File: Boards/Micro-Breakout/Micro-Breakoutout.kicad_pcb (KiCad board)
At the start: 2 copper layers, 92.7 x 54.6 mm, 38 parts, among them J1 Conn_01x04, J10 Conn_01x17, J11 Conn_01x04, J12 Conn_01x04, J13 Conn_01x02, J14 Conn_01x04, J16 Conn_01x04, J17 Conn_01x04, J18 Conn_01x04, J2 Conn_01x04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

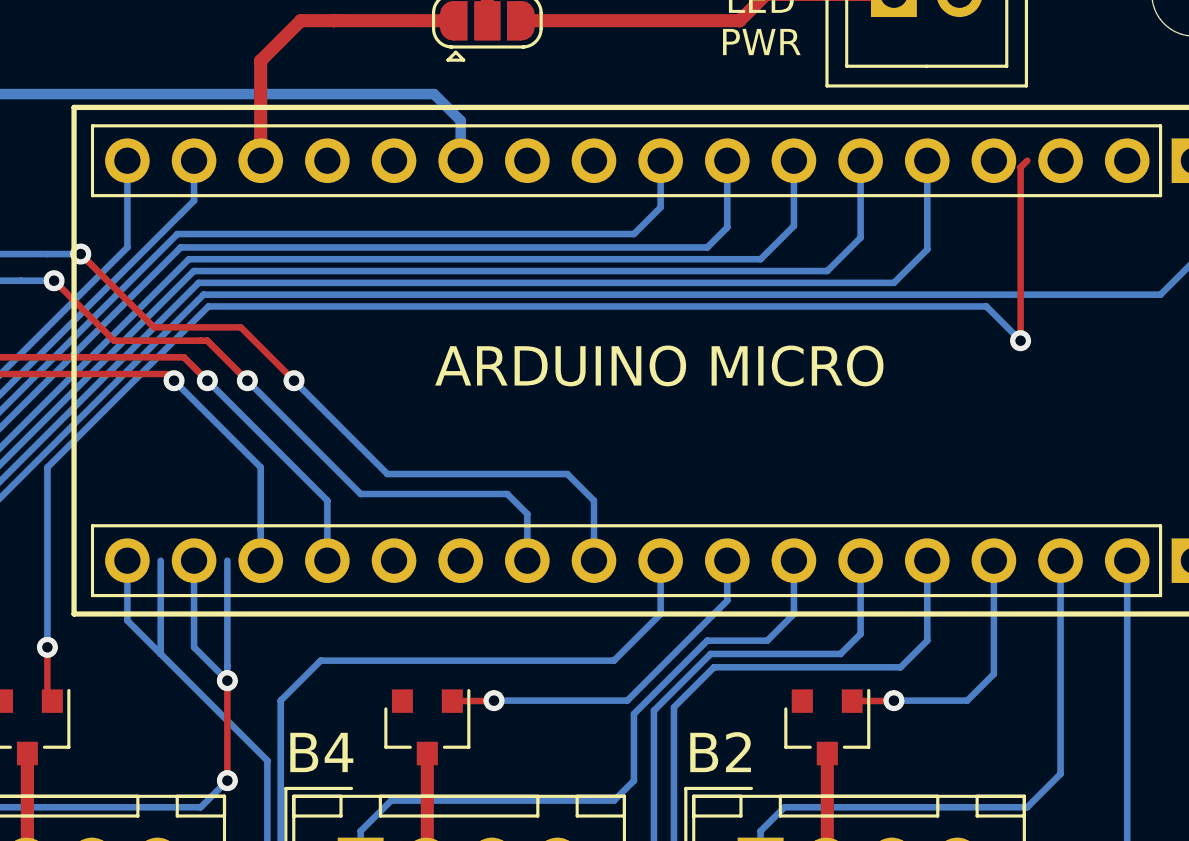
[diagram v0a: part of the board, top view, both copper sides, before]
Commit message: Fixed broken trace on Micro Breakout
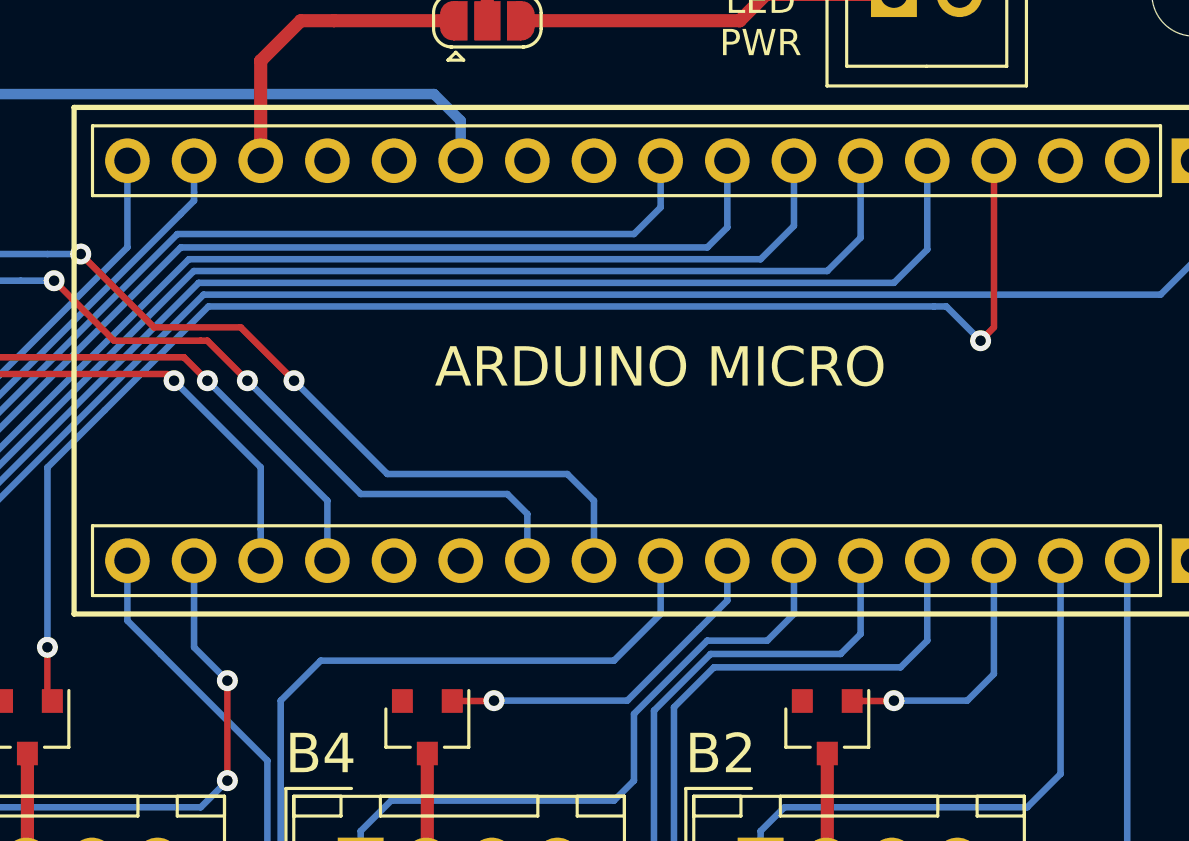
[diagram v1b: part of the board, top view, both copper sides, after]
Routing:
- net /B6: track 25.6 -> 21.0 mm
- net /B5LED: track 31.1 -> 27.5 mm
- net /B6LED: track 56.1 -> 54.7 mm
